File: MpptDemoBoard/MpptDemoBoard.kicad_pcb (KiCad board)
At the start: 2 copper layers, 48.4 x 34.4 mm, 21 parts, among them IC1 SPV1040T, U1 282837-2, U2 282837-2

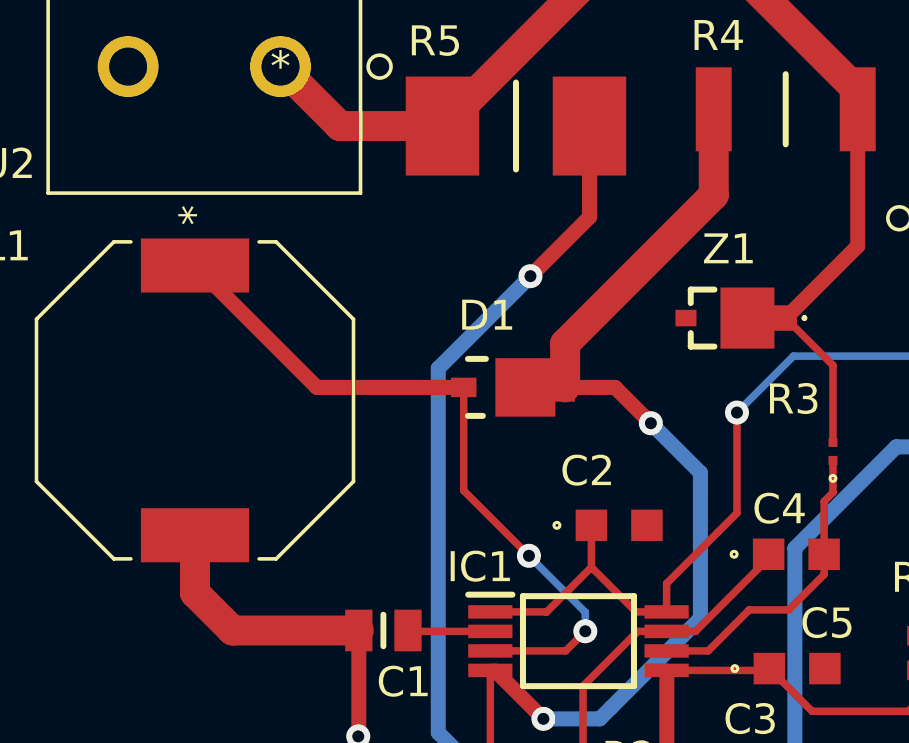
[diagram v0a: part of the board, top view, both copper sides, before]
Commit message: Updated pcb with new diode
replaced diode STPS120MF (If=1A) with STPS2150A (If=2A). Updated symbol and footprint library and docs containing schematic, pcb layout image and 3d image.
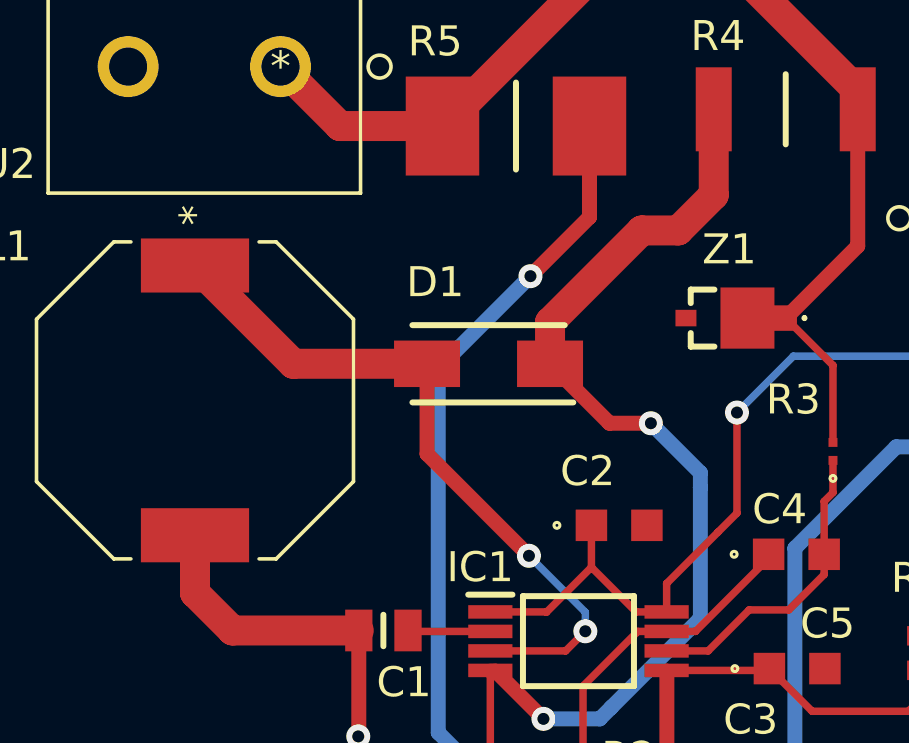
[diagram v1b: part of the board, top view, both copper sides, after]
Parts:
- D1: value STPS120MF -> STPS2150A; footprint myfootprints:STPS120MF -> myfootprints:STPS2150A
- moved D1 1.13 mm to (120.7, 112.8), turned to 180 degrees
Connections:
- D1 pad 1: Net-(D1-Pad1) -> Net-(C3-Pad1)
- D1 pad 2: Net-(C3-Pad1) -> Net-(IC1-Pad3)
- IC1 pad 3: Net-(D1-Pad1) -> Net-(IC1-Pad3)
- L1 pad 1: Net-(D1-Pad1) -> Net-(IC1-Pad3)
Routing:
- net Net-(D1-Pad1): track 23.9 -> 0.00 mm, vias 2 -> 0
- net Net-(IC1-Pad3): track 0.00 -> 23.6 mm, vias 0 -> 2

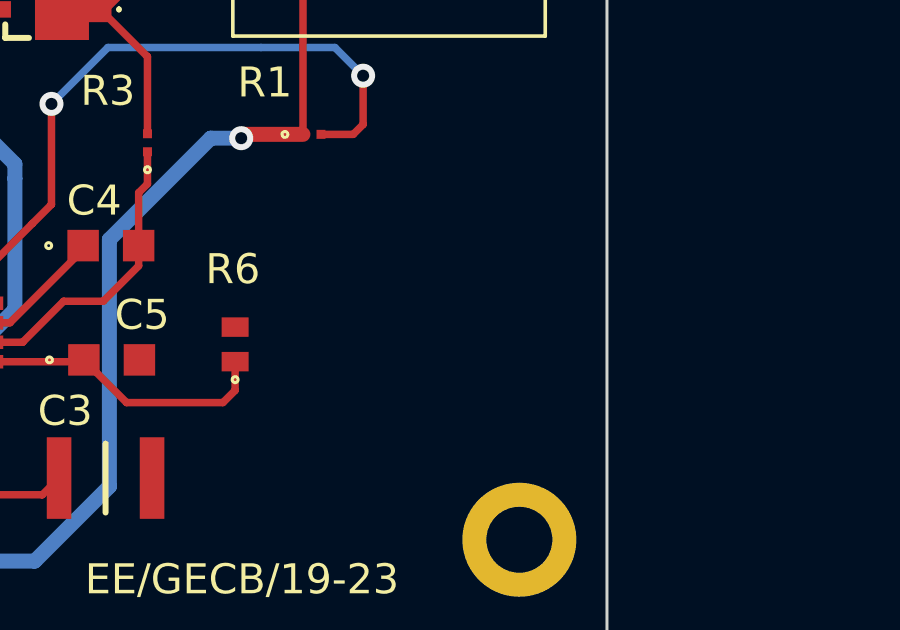
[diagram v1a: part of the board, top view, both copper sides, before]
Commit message: Updated BOM
BOM updated with diode stps2150a
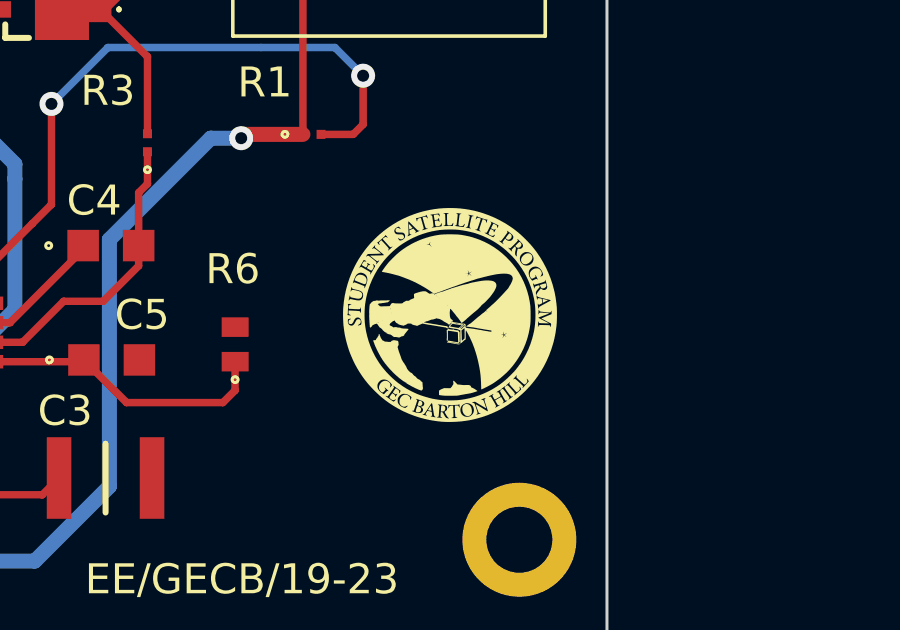
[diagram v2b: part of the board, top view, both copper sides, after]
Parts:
- added G***: LOGO, LOGO, F.Cu at (142.2, 121.5)
